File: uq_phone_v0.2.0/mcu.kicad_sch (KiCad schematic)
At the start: 22 parts, among them J6 Conn_ARM_SWD_TagConnect_TC2030, U5 TXB0108RGYR, U6 TXB0108RGYR, U7 STM32H733VGTx

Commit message: Clean repo
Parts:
- removed U7: STM32H733VGTx, Package_QFP:LQFP-100_14x14mm_P0.5mm, symbol MCU_ST_STM32H7:STM32H733VGTx
- added U6: STM32H733VGHx, Package_BGA:TFBGA-100_8x8mm_Layout10x10_P0.8mm, symbol MCU_ST_STM32H7:STM32H733VGHx
- renumbered C19 to C14, C22 to C15, C23 to C16, C24 to C17, C25 to C18, C26 to C19, C18 to C20, C14 to C21, C16 to C22, C15 to C23, C17 to C24, C20 to C25, C21 to C26, R49 to R20, R24 to R21, R25 to R22, R26 to R23, R27 to R24, U6 to U7
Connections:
- net +3.3V: now also U6.B2 (VBAT), U6.D2 (VDD), U6.F4 (VDD), U6.F5 (VDD), U6.H1 (VDDA), U6.K1 (VDD)
- net AUD_SW_H: now also U6.J4 (PB0)
- net DISP_BL: now also U6.J7 (PB10)
- net DISP_CS: now also U6.D6 (PD7)
- net DISP_DB0: now also U6.H8 (PD14)
- net DISP_DB1: now also U6.G8 (PD15)
- net DISP_DB10: now also U6.K6 (PE13)
- net DISP_DB11: now also U6.G7 (PE14)
- net DISP_DB12: now also U6.H7 (PE15)
- net DISP_DB13: now also U6.K9 (PD8)
- net DISP_DB14: now also U6.J9 (PD9)
- net DISP_DB15: now also U6.H9 (PD10)
- net DISP_DB2: now also U6.D8 (PD0)
- net DISP_DB3: now also U6.E8 (PD1)
- net DISP_DB4: now also U6.H5 (PE7)
- net DISP_DB5: now also U6.J5 (PE8)
- net DISP_DB6: now also U6.K5 (PE9)
- net DISP_DB7: now also U6.G6 (PE10)
- net DISP_DB8: now also U6.H6 (PE11)
- net DISP_DB9: now also U6.J6 (PE12)
- net DISP_DC: now also U6.G9 (PD11)
- net DISP_RD: now also U6.D7 (PD4)
- net DISP_RES: now also U6.C7 (PD3)
- net DISP_WR: now also U6.B6 (PD5)
- net FUEL_GPO: now also U6.K8 (PB12)
- net GND: now also U6.C2 (VSS), U6.E4 (VSS), U6.E5 (VSS), U6.E6 (VSS), U6.G1 (VSSA), U6.J1 (VSS)
- net HP_DET_MCU: now also U6.H4 (PC5)
- net LED_DATA: now also U6.K2 (PA3)
- net MCP_PG: now also U6.J8 (PB13)
- net MCP_STAT1: now also U6.G10 (PB15)
- net MCP_STAT2: now also U6.H10 (PB14)
- net MCU_AUD_BCLK_H: now also U6.H3 (PA5)
- net MCU_AUD_OUT_L_H: now also U6.K3 (PA7)
- net MCU_AUD_SYNC_H: now also U6.G3 (PA4)
- net MCU_CTS: now also U6.C10 (PA11)
- net MCU_DCD: now also U6.K10 (PD12)
- net MCU_DSR: now also U6.D9 (PA8)
- net MCU_DTR: now also U6.J10 (PD13)
- net MCU_RI: now also U6.F10 (PC6)
- net MCU_RTS: now also U6.B10 (PA12)
- net MCU_RXD: now also U6.D10 (PA10)
- net MCU_TXD: now also U6.C9 (PA9)
- net MOB_PWR_CTL: now also U6.G5 (PB2)
- net MOB_RST_CTL: now also U6.K7 (PB11)
- net MOB_WAKE_H: now also U6.K4 (PB1)
- net PB_0: now also U6.C4 (PE1)
- net PB_1: now also U6.B3 (PE3)
- net PB_2: now also U6.C3 (PE4)
- net PB_3: now also U6.D3 (PE5)
- net PB_4: now also U6.E3 (PE6)
- net PB_5: now also U6.A2 (PC13)
- net PB_6: now also U6.A1 (PC14)
- net PB_7: now also U6.B1 (PC15)
- net PB_8: now also U6.C1 (PH0)
- net PB_9: now also U6.D1 (PH1)
- net PB_CALL: now also U6.C6 (PD6)
- net PB_DPAD_DOWN: now also U6.A6 (PB4(NJTRST))
- net PB_DPAD_LEFT: now also U6.B5 (PB6)
- net PB_DPAD_RIGHT: now also U6.C5 (PB5)
- net PB_DPAD_SELECT: now also U6.A5 (PB7)
- net PB_DPAD_UP: now also U6.A7 (PB3(JTDO)
- net PB_END_CALL: now also U6.A8 (PA15(JTDI))
- net PB_HASH: now also U6.A3 (PE2)
- net PB_MENU_L: now also U6.F1 (PC0)
- net PB_MENU_R: now also U6.F2 (PC1)
- net PB_PWR: now also U6.G2 (PA0)
- net PB_STAR: now also U6.D4 (PE0)
- net PB_VOL_DOWN: now also U6.H2 (PA1)
- net PB_VOL_UP: now also U6.J2 (PA2)
- net RST: now also U6.E1 (NRST)
- net SCL: now also U6.B4 (PB8)
- net SDA: now also U6.A4 (PB9)
- net SWCLK: now also U6.A9 (PA14(JTCK)
- net SWDIO: now also U6.A10 (PA13(JTMS)
- net VIB_EN: now also U6.G4 (PC4)
- net VIB_PWM: now also U6.J3 (PA6)
- net uSD_CLK: now also U6.C8 (PC12)
- net uSD_CMD: now also U6.B7 (PD2)
- net uSD_DAT0: now also U6.F9 (PC8)
- net uSD_DAT1: now also U6.E9 (PC9)
- net uSD_DAT2: now also U6.B9 (PC10)
- net uSD_DAT3: now also U6.B8 (PC11)
- net uSD_DET: now also U6.E10 (PC7)
- net at C26.1: now also U6.F8 (VCAP)
- net at R20.2: now also U6.D5 (BOOT0)
- net at C25.1: now also U6.E7 (VCAP)
- no-connect marks 6 -> 5

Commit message: Add more footprints, reduce sizes
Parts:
- C14: footprint Capacitor_SMD:C_0402_1005Metric -> Capacitor_SMD:C_0201_0603Metric; LCSC PN C191541 -> C335103
- C15, C16, C17, C18, C19, C20, C21, C22, C23, C24: footprint Capacitor_SMD:C_0402_1005Metric -> Capacitor_SMD:C_0201_0603Metric; LCSC PN C307331 -> C160831
- R20, R23, R24: footprint Resistor_SMD:R_0402_1005Metric -> Resistor_SMD:R_0201_0603Metric; LCSC PN C851848 -> C106225
- R21, R22: footprint Resistor_SMD:R_0402_1005Metric -> Resistor_SMD:R_0201_0603Metric; LCSC PN C606173 -> C138135

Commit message: Various Changes to footprints and components
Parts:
- removed U5, U7: TXB0108RGYR, TXB0108RGYR:IC_TXB0108RGYR, symbol TXB0108RGYR:TXB0108RGYR
- added U5, U7: TXB0108YZPR2, TXB0108YZPR2:YZP20, symbol TXB0108YZPR2:TXB0108YZPR2
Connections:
- net +1.8V: now also U5.C4 (VCCA), U5.D4 (OE), U7.C4 (VCCA), U7.D4 (OE)
- net +3.3V: now also U5.C1 (VCCB), U7.C1 (VCCB)
- net AUD_SCL: now also U7.A4 (A2)
- net AUD_SDA: now also U7.A3 (A1)
- net AUD_SW_H: now also U7.E1 (B6)
- net AUD_SW_L: now also U7.E4 (A6)
- net GND: now also U5.D1 (GND), U7.D1 (GND)
- net HP_DET: now also U7.B4 (A4)
- net HP_DET_MCU: now also U7.B1 (B4)
- net MCU_AUD_BCLK_H: now also U7.D2 (B7)
- net MCU_AUD_BCLK_L: now also U7.D3 (A7)
- net MCU_AUD_OUT_L: now also U7.E3 (A8)
- net MCU_AUD_OUT_L_H: now also U7.E2 (B8)
- net MCU_AUD_SYNC_H: now also U7.C2 (B5)
- net MCU_AUD_SYNC_L: now also U7.C3 (A5)
- net MCU_CTS: now also U5.E1 (B6)
- net MCU_DCD: now also U5.A1 (B2)
- net MCU_DSR: now also U5.A2 (B1)
- net MCU_DTR: now also U5.B2 (B3)
- net MCU_RI: now also U5.E2 (B8)
- net MCU_RTS: now also U5.D2 (B7)
- net MCU_RXD: now also U5.B1 (B4)
- net MCU_TXD: now also U5.C2 (B5)
- net MOB_CTS: now also U5.E4 (A6)
- net MOB_DCD: now also U5.A4 (A2)
- net MOB_DSR: now also U5.A3 (A1)
- net MOB_DTR: now also U5.B3 (A3)
- net MOB_RI: now also U5.E3 (A8)
- net MOB_RTS: now also U5.D3 (A7)
- net MOB_RXD: now also U5.B4 (A4)
- net MOB_TXD: now also U5.C3 (A5)
- net MOB_WAKE_H: now also U7.B2 (B3)
- net MOB_WAKE_L: now also U7.B3 (A3)
- net SCL: now also U7.A1 (B2)
- net SDA: now also U7.A2 (B1)
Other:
- title: Power System -> UQ Phone
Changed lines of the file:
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@@
 	(paper "A3")
 	(title_block
-		(title "Power System")
+		(title "UQ Phone")
+		(rev "0.2.0")
 		(company "The University of Queensland")
 	)

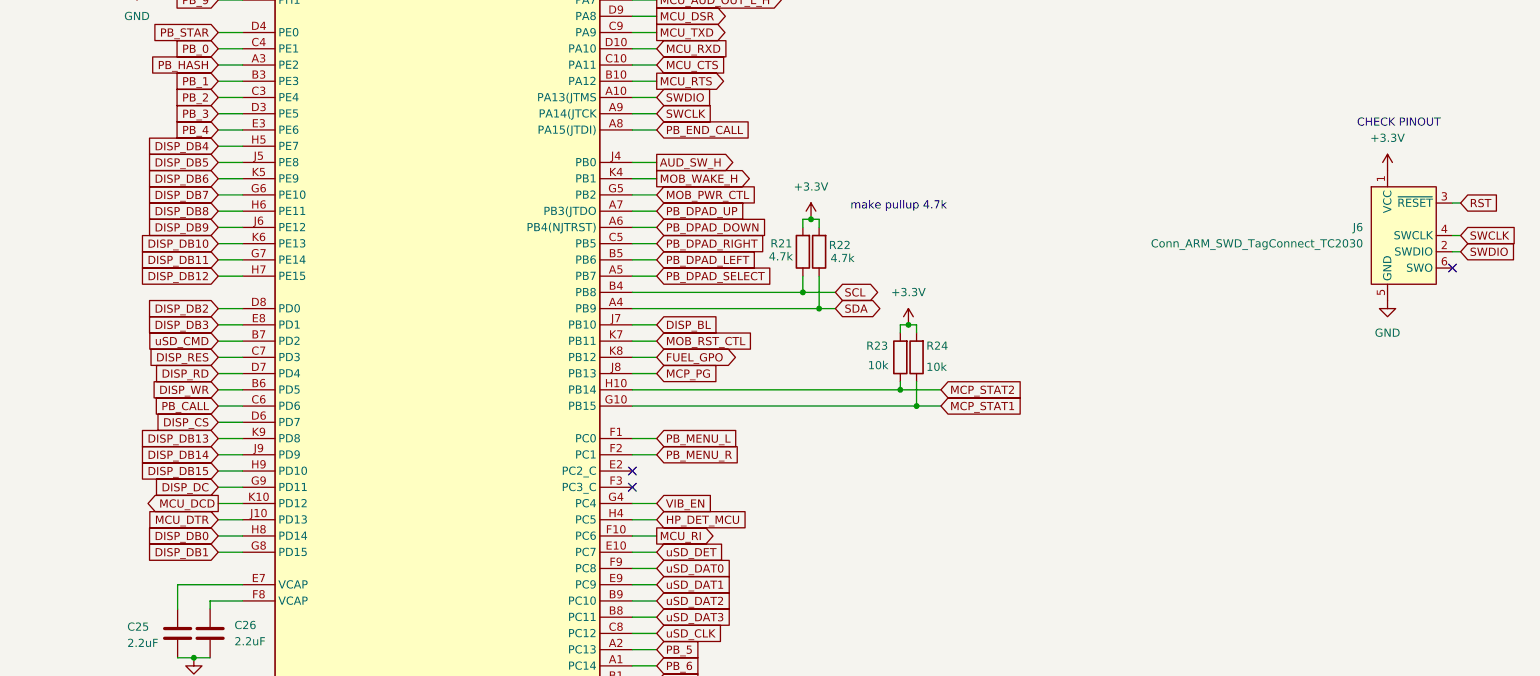
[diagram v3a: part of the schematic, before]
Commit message: Minor Changes - new display
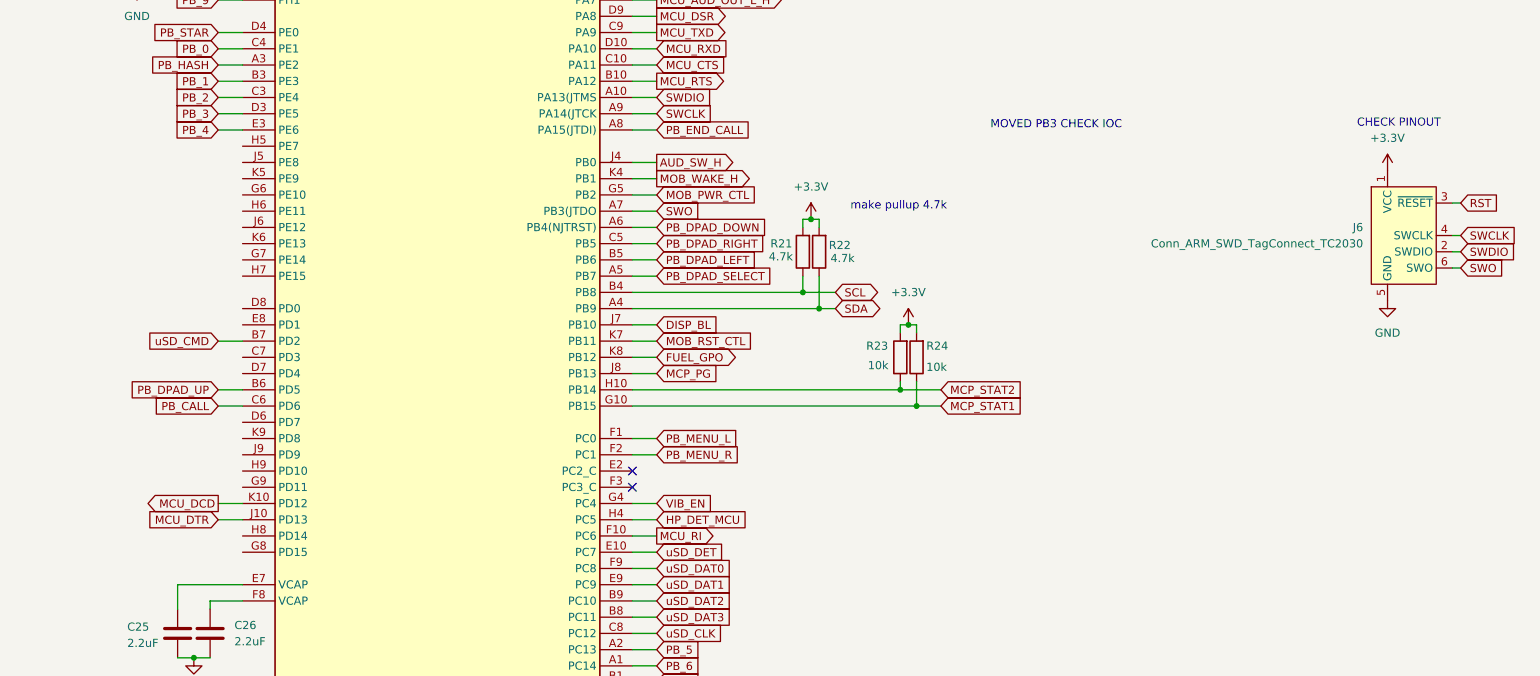
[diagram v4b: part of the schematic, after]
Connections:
- net DISP_WR is gone; now on net PB_DPAD_UP: U6.B6 (PD5)
- net PB_DPAD_UP: no longer U6.A7 (PB3(JTDO)
- net SWO: now reaches J6.6 (SWO)
- net SWO: now also U6.A7 (PB3(JTDO)
- net DISP_CS: no longer names the net of U6.D6 (PD7)
- net DISP_DB0: no longer names the net of U6.H8 (PD14)
- net DISP_DB1: no longer names the net of U6.G8 (PD15)
- net DISP_DB10: no longer names the net of U6.K6 (PE13)
- net DISP_DB11: no longer names the net of U6.G7 (PE14)
- net DISP_DB12: no longer names the net of U6.H7 (PE15)
- net DISP_DB13: no longer names the net of U6.K9 (PD8)
- net DISP_DB14: no longer names the net of U6.J9 (PD9)
- net DISP_DB15: no longer names the net of U6.H9 (PD10)
- net DISP_DB2: no longer names the net of U6.D8 (PD0)
- net DISP_DB3: no longer names the net of U6.E8 (PD1)
- net DISP_DB4: no longer names the net of U6.H5 (PE7)
- net DISP_DB5: no longer names the net of U6.J5 (PE8)
- net DISP_DB6: no longer names the net of U6.K5 (PE9)
- net DISP_DB7: no longer names the net of U6.G6 (PE10)
- net DISP_DB8: no longer names the net of U6.H6 (PE11)
- net DISP_DB9: no longer names the net of U6.J6 (PE12)
- net DISP_DC: no longer names the net of U6.G9 (PD11)
- net DISP_RD: no longer names the net of U6.D7 (PD4)
- net DISP_RES: no longer names the net of U6.C7 (PD3)
- no-connect marks 5 -> 4
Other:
- note added: "MOVED PB3 CHECK IOC"

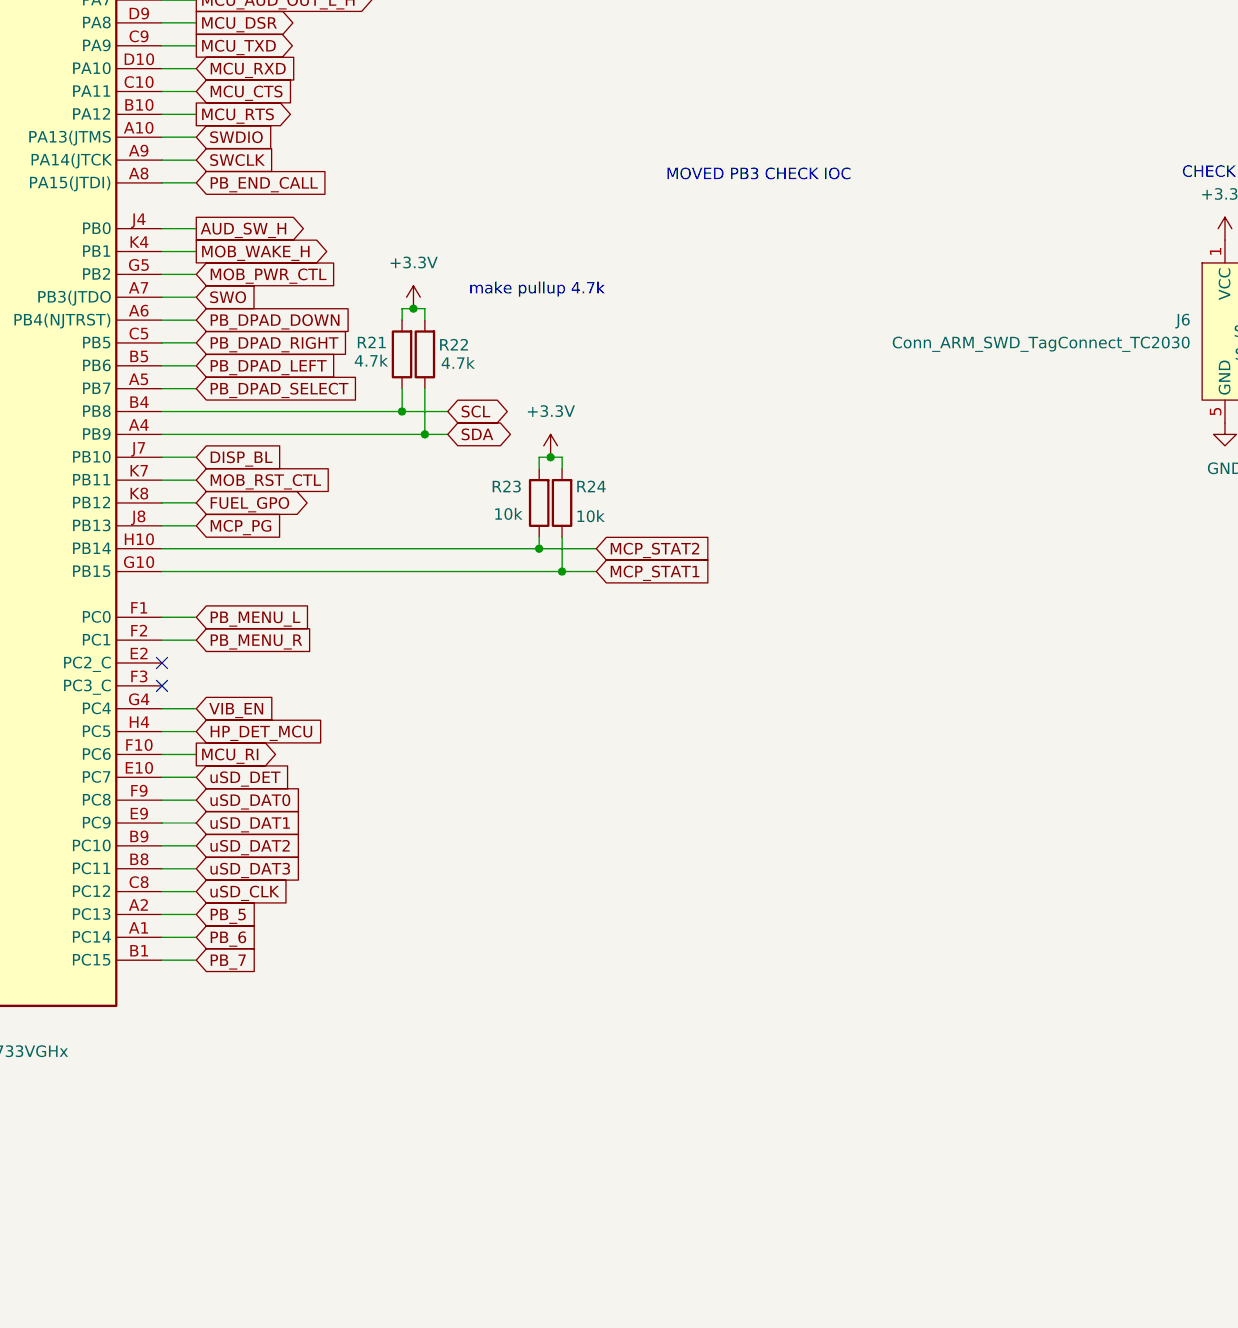
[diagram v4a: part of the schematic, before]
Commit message: New HP jack, move stuff out for new arrangement
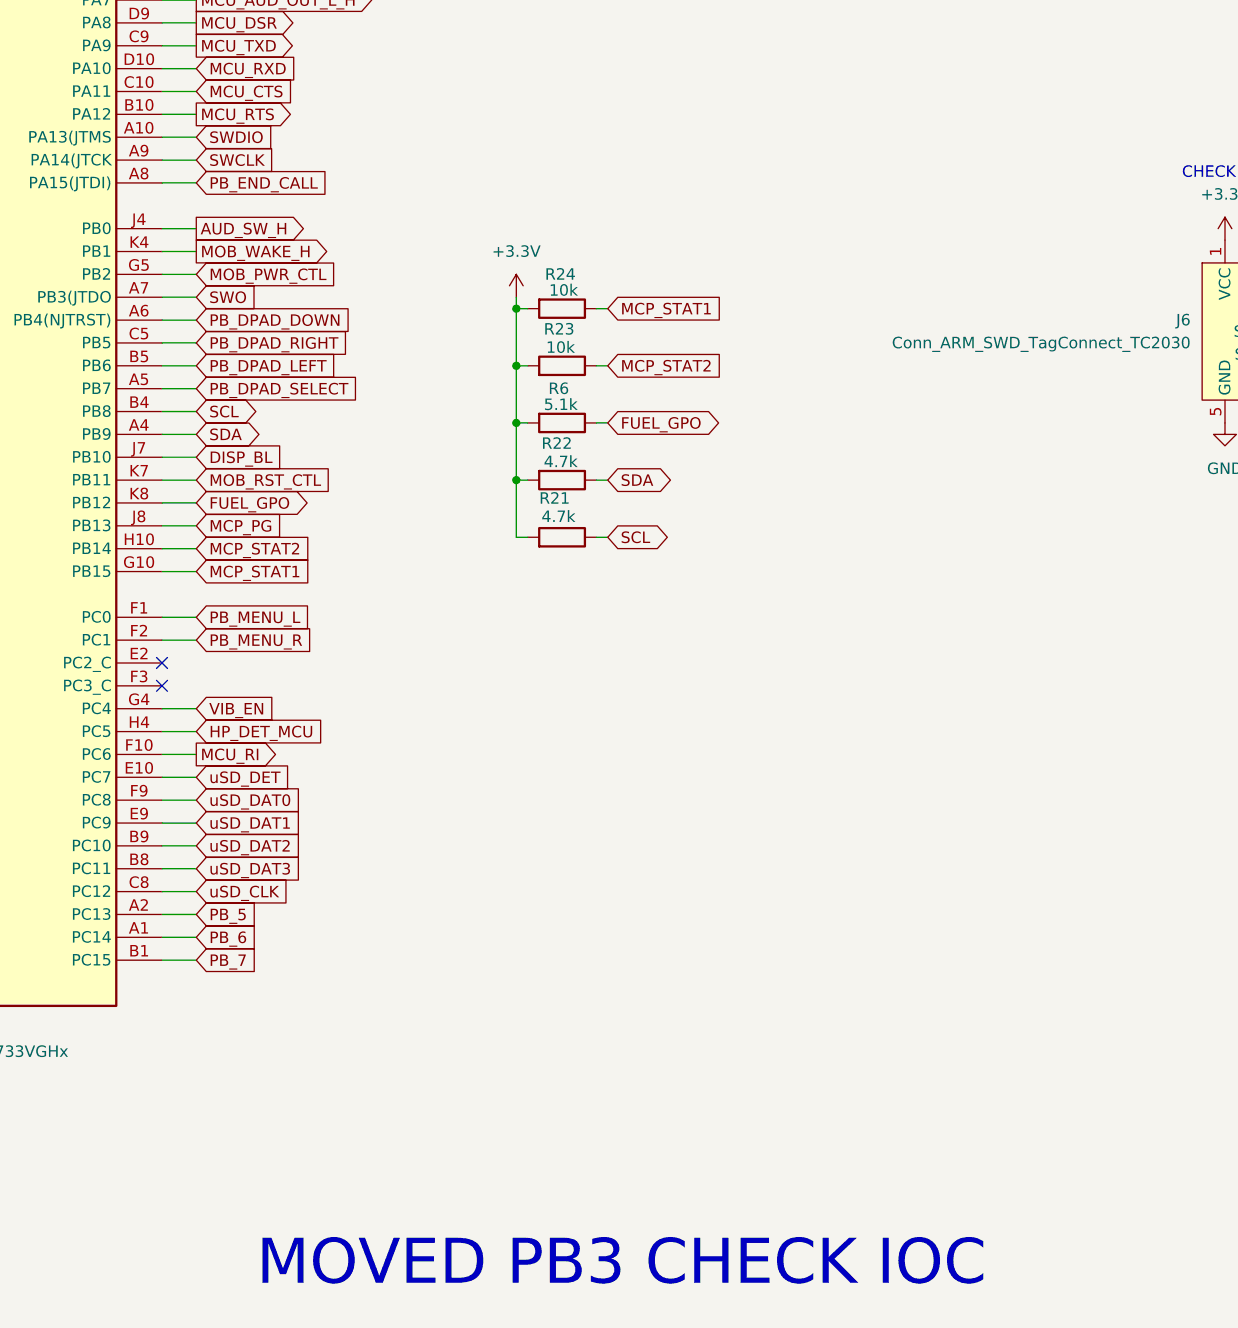
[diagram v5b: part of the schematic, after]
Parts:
- added R6: 5.1k, Resistor_SMD:R_0201_0603Metric, symbol Resistors:Resistor_5k1
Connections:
- net +3.3V: now also R6.2
- net FUEL_GPO: now also R6.1
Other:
- note removed: "make pullup 4.7k"
- moved on the sheet: R21, R22, R23, R24

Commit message: New Layout
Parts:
- removed R21: 4.7k, Resistor_SMD:R_0201_0603Metric, symbol Resistors:Resistor_4k7
- removed U5: TXB0108YZPR2, TXB0108YZPR2:YZP20, symbol TXB0108YZPR2:TXB0108YZPR2
- added C50, C51: 100nF, Capacitor_SMD:C_0201_0603Metric, symbol Capacitors:capacitor_100nF
- added J7, J9: 559092474, 559092474:CON_559092474, symbol 559092474:559092474
- added Q1, Q2: MMBT3904LP-7, MMBT3904LP-7:DFN101X61X53-3N, symbol MMBT3904LP-7:MMBT3904LP-7
- added R16, R17, R4: 4.7k, Resistor_SMD:R_0201_0603Metric, symbol Resistors:Resistor_4k7
- added R18, R19: 47k, Resistor_SMD:R_0201_0603Metric, symbol Resistors:Resistor_47k
- added U16: TXB0108YZPR2, TXB0108YZPR2:YZP20, symbol TXB0108YZPR2:TXB0108YZPR2
- added U5: TCA9509MRVHR, TCA9509MRVHR:RVH8_0P4X0P4, symbol TCA9509MRVHR:TCA9509MRVHR
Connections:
- net +1.8V: now also C50.1, J7.10, J7.11, J7.12, J7.9, U16.C4 (VCCA), U16.D4 (OE), U5.1 (VCCA), U5.5 (EN)
- net +3.3V: now also C51.1, R4.2, U16.C1 (VCCB), U5.8 (VCCB)
- net AUD_SCL: now also U5.2 (SCLA); no longer U7.A4 (A2)
- net AUD_SDA: now also U5.3 (SDAA); no longer U7.A3 (A1)
- net GND: now also C50.2, C51.2, J7.13, J7.14, J7.15, J7.16, J7.17, J7.18, J7.19, J7.20, J7.21, J7.22, J7.23, J7.24, J7.P1, J7.P2, J7.P3, J7.P4, Q1.2, Q2.2, R18.1, R19.1, U16.D1 (GND), U5.4 (GND), U5.9 (EPAD)
- net MCU_CTS: now also U16.E1 (B6)
- net MCU_DCD: now also U16.A1 (B2)
- net MCU_DSR: now also U16.A2 (B1)
- net MCU_DTR: now also U16.B2 (B3)
- net MCU_RI: now also U16.E2 (B8)
- net MCU_RTS: now also U16.D2 (B7)
- net MCU_RXD: now also U16.B1 (B4)
- net MCU_TXD: now also U16.C2 (B5)
- net MOB_CTS: now also U16.E4 (A6)
- net MOB_DCD: now also U16.A4 (A2)
- net MOB_DSR: now also U16.A3 (A1)
- net MOB_DTR: now also U16.B3 (A3)
- net MOB_PWR_CTL: now also R16.2
- net MOB_RI: now also U16.E3 (A8)
- net MOB_RST_CTL: now also R17.2
- net MOB_RTS: now also U16.D3 (A7)
- net MOB_RXD: now also U16.B4 (A4)
- net MOB_TXD: now also U16.C3 (A5)
- net SCL: now also R22.1, U5.7 (SCLB); no longer U7.A1 (B2)
- net SDA: now also R4.1, U5.6 (SDAB); no longer R22.1, U7.A2 (B1)
- new net: Q1.1, R16.1, R18.2
- new net: Q2.1, R17.1, R19.2
- new net MOB_PWR: Q1.3
- new net MOB_RST: Q2.3
- new net VBAT: J7.1, J7.2, J7.3, J7.4, J7.5, J7.6, J7.7, J7.8
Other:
- moved on the sheet: C14, C15, C16, C17, C18, C19, C20, C21, C22, C23, C24, C25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
